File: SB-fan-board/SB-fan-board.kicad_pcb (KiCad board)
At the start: 2 copper layers, 51.6 x 35.1 mm, 28 parts, among them J1 FAN0, J2 FAN1, J3 NEO, J4 MAIN, U1 LMR33610BDDAR, U2 TPS565208

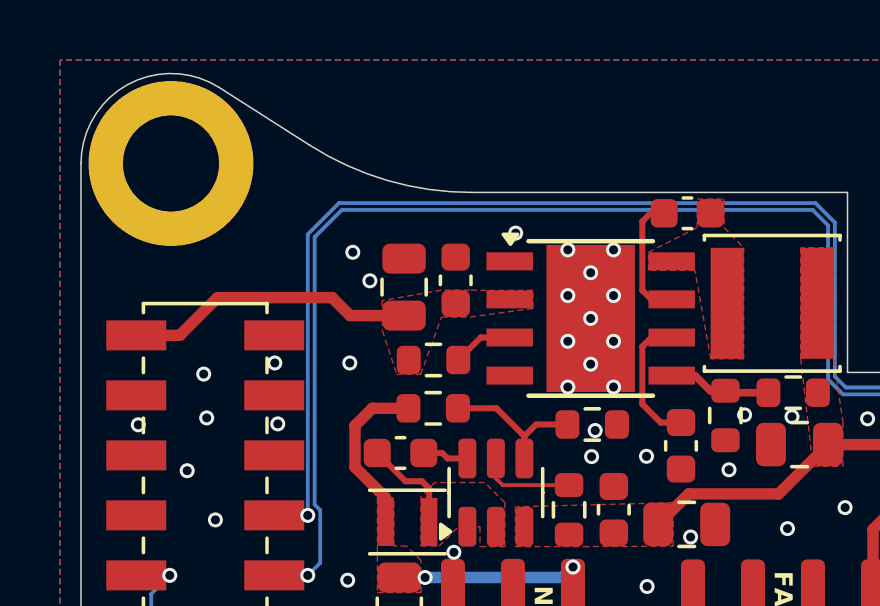
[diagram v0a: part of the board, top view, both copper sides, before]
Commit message: footprint: change input cap to 1206
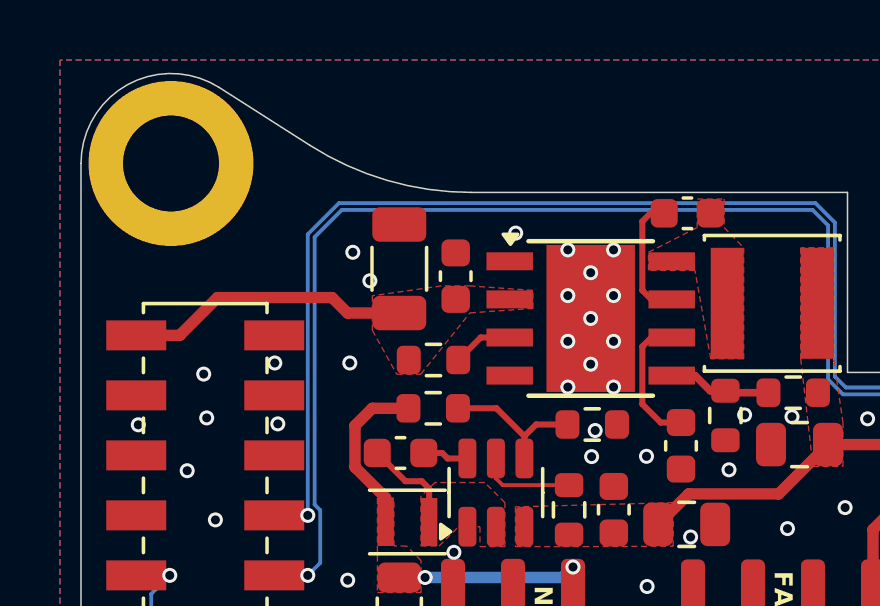
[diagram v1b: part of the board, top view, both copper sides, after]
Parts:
- C2: footprint Capacitor_SMD:C_0805_2012Metric -> Capacitor_SMD:C_1206_3216Metric
- moved C2 0.63 mm to (152.8, 74.7)
- moved C3 0.14 mm to (154.7, 75.0)
